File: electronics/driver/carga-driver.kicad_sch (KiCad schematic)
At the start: 74 parts, among them J1 USB2UART, J2 1.47 IPS LCD, J3 ConnBattery, J4 RTD_PT100, Q1 SS8050, Q2 SS8050, Q3 SS8050, SW1 RST, SW2 IN1, SW3 Boot, SW4 IN2, SW5 IN4, SW6 IN4, SW7 IN5, U1 CH340C, U2 ESP32-S3-WROOM-1, U3 TPS63001_SEPIC_3V3, U4 MAX31865xTP, U5 BQ24075RGT_DPPM, U6 HX711

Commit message: feat: create l298, mcp23017 driver module
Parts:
- removed C10: 22uF, Capacitor_SMD:C_0805_2012Metric_Pad1.18x1.45mm_HandSolder, symbol Device:C
- removed C11, C15: 1uF, Capacitor_SMD:C_0805_2012Metric_Pad1.18x1.45mm_HandSolder, symbol Device:C
- removed C12, C18, C19, C20, C3, C4, C5, C6, C7, C8, C9: 100nF, Capacitor_SMD:C_0805_2012Metric_Pad1.18x1.45mm_HandSolder, symbol Device:C
- removed C13, C16, C17: 10uF, Capacitor_SMD:C_0805_2012Metric_Pad1.18x1.45mm_HandSolder, symbol Device:C
- removed C14: 0.1uF, Capacitor_SMD:C_0805_2012Metric_Pad1.18x1.45mm_HandSolder, symbol Device:C
- removed C22, C23: 4.7uF, Capacitor_SMD:C_0805_2012Metric_Pad1.18x1.45mm_HandSolder, symbol Device:C
- removed D1: INDICATOR, LED_SMD:LED_1206_3216Metric_Pad1.42x1.75mm_HandSolder, symbol Device:LED
- removed D2: VDD, LED_SMD:LED_1206_3216Metric_Pad1.42x1.75mm_HandSolder, symbol Device:LED
- removed D3: green, LED_SMD:LED_0805_2012Metric_Pad1.15x1.40mm_HandSolder, symbol Device:LED
- removed D4: red, LED_SMD:LED_0805_2012Metric_Pad1.15x1.40mm_HandSolder, symbol Device:LED
- removed H1, H2, H3, H4: MountingHole, MountingHole:MountingHole_2mm, symbol Mechanical:MountingHole
- removed J1: USB2UART, Connector_USB:USB_C_Receptacle_GCT_USB4110, symbol Connector:USB_C_Receptacle_USB2.0_14P
- removed J2: 1.47 IPS LCD, Connector_PinHeader_2.54mm:PinHeader_1x08_P2.54mm_Vertical, symbol Connector_Generic:Conn_01x08
- removed J3: ConnBattery, Connector_PinHeader_2.54mm:PinHeader_1x03_P2.54mm_Vertical, symbol Connector_Generic:Conn_01x03
- removed J4: RTD_PT100, TerminalBlock_Phoenix:TerminalBlock_Phoenix_PT-1,5-3-5.0-H_1x03_P5.00mm_Horizontal, symbol Connector:Screw_Terminal_01x03
- removed JP1: 3_OR_2_Wire, Jumper:SolderJumper-3_P1.3mm_Open_RoundedPad1.0x1.5mm, symbol Jumper:SolderJumper_3_Open
- removed JP2: 2_Wire, Jumper:SolderJumper-2_P1.3mm_Open_TrianglePad1.0x1.5mm, symbol Jumper:SolderJumper_2_Open
- removed L1: 22uH 1A, Inductor_SMD:L_Bourns_SRP7028A_7.3x6.6mm, symbol Device:L
- removed Q1, Q2, Q3: SS8050, Package_TO_SOT_SMD:SOT-23_Handsoldering, symbol Transistor_BJT:BC817
- removed R1, R10, R13, R14, R2, R3, R4, R7, R8, R9: 1k, Resistor_SMD:R_0805_2012Metric_Pad1.20x1.40mm_HandSolder, symbol Device:R_US
- removed R11, R12: 10k, Resistor_SMD:R_0805_2012Metric_Pad1.20x1.40mm_HandSolder, symbol Device:R_US
- removed R15: 100, Resistor_SMD:R_0805_2012Metric_Pad1.20x1.40mm_HandSolder, symbol Device:R_US
- removed R16: 46.4K, Resistor_SMD:R_0805_2012Metric_Pad1.20x1.40mm_HandSolder, symbol Device:R_US
- removed R17: 2K2, Resistor_SMD:R_0805_2012Metric_Pad1.20x1.40mm_HandSolder, symbol Device:R_US
- removed R18: 1.13k, Resistor_SMD:R_0805_2012Metric_Pad1.20x1.40mm_HandSolder, symbol Device:R_US
- removed R19: 400 1%, Resistor_SMD:R_0805_2012Metric_Pad1.20x1.40mm_HandSolder, symbol Device:R_US
- removed R20, R21: 1K5, Resistor_SMD:R_0805_2012Metric_Pad1.20x1.40mm_HandSolder, symbol Device:R_US
- removed R5, R6: 5K1, Resistor_SMD:R_0805_2012Metric_Pad1.20x1.40mm_HandSolder, symbol Device:R_US
- removed SW1: RST, Button_Switch_SMD:SW_SPST_PTS810, symbol Switch:SW_Push
- removed SW2: IN1, Button_Switch_SMD:SW_SPST_Omron_B3FS-100xP, symbol Switch:SW_Push
- removed SW3: Boot, Button_Switch_SMD:SW_SPST_PTS810, symbol Switch:SW_Push
- removed SW4: IN2, Button_Switch_SMD:SW_SPST_Omron_B3FS-100xP, symbol Switch:SW_Push
- removed SW5, SW6: IN4, Button_Switch_SMD:SW_SPST_Omron_B3FS-100xP, symbol Switch:SW_Push
- removed SW7: IN5, Button_Switch_SMD:SW_SPST_Omron_B3FS-100xP, symbol Switch:SW_Push
- removed U1: CH340C, Package_SO:SOIC-16_3.9x9.9mm_P1.27mm, symbol Interface_USB:CH340C
- removed U2: ESP32-S3-WROOM-1, RF_Module:ESP32-S3-WROOM-1, symbol RF_Module:ESP32-S3-WROOM-1
- removed U3: TPS63001_SEPIC_3V3, Package_SON:Texas_DRC0010J_ThermalVias, symbol Regulator_Switching:TPS63001
- removed U4: MAX31865xTP, Package_DFN_QFN:TQFN-20-1EP_5x5mm_P0.65mm_EP3.25x3.25mm, symbol Sensor_Temperature:MAX31865xTP
- removed U5: BQ24075RGT_DPPM, Package_DFN_QFN:VQFN-16-1EP_3x3mm_P0.5mm_EP1.6x1.6mm, symbol Battery_Management:BQ24075RGT
- removed U6: HX711, Package_SO:SOIC-16_3.9x9.9mm_P1.27mm, symbol Analog_ADC:HX711
- added C21, C24, C25, C26: 100nF, Capacitor_SMD:C_0805_2012Metric_Pad1.18x1.45mm_HandSolder, symbol Device:C
- added D10, D11, D12, D13, D14, D15, D16, D17, D18, D19, D20, D5, D6, D7, D8, D9: 1N4007, Diode_THT:D_DO-41_SOD81_P10.16mm_Horizontal, symbol Diode:1N4007
- added J1: ServoConn, TerminalBlock_Phoenix:TerminalBlock_Phoenix_PT-1,5-3-5.0-H_1x03_P5.00mm_Horizontal, symbol Connector:Screw_Terminal_01x03
- added J10: LimitSw1, TerminalBlock_Phoenix:TerminalBlock_Phoenix_PT-1,5-4-5.0-H_1x04_P5.00mm_Horizontal, symbol Connector:Screw_Terminal_01x04
- added J11: LimitSw2, TerminalBlock_Phoenix:TerminalBlock_Phoenix_PT-1,5-4-5.0-H_1x04_P5.00mm_Horizontal, symbol Connector:Screw_Terminal_01x04
- added J12: LimitSwCommon, TerminalBlock_Phoenix:TerminalBlock_Phoenix_PT-1,5-2-5.0-H_1x02_P5.00mm_Horizontal, symbol Connector:Screw_Terminal_01x02
- added J2: DriverConn2, Connector_IDC:IDC-Header_2x05_P2.54mm_Vertical, symbol Connector_Generic:Conn_02x05_Odd_Even
- added J5: DriverConn, Connector_IDC:IDC-Header_2x05_P2.54mm_Vertical, symbol Connector_Generic:Conn_02x05_Odd_Even
- added J7: MotorConn2_3, TerminalBlock_Phoenix:TerminalBlock_Phoenix_PT-1,5-4-5.0-H_1x04_P5.00mm_Horizontal, symbol Connector:Screw_Terminal_01x04
- added J8: SolenoidConn, TerminalBlock_Phoenix:TerminalBlock_Phoenix_PT-1,5-2-5.0-H_1x02_P5.00mm_Horizontal, symbol Connector:Screw_Terminal_01x02
- added J9: MotorConn1, TerminalBlock_Phoenix:TerminalBlock_Phoenix_PT-1,5-2-5.0-H_1x02_P5.00mm_Horizontal, symbol Connector:Screw_Terminal_01x02
- added R22, R23, R24: 4K7, Resistor_SMD:R_0805_2012Metric_Pad1.20x1.40mm_HandSolder, symbol Device:R_US
- added R25, R26, R27, R28: 1, Resistor_SMD:R_0805_2012Metric_Pad1.20x1.40mm_HandSolder, symbol Device:R_US
- added U10, U7: L298HN, Package_TO_SOT_THT:TO-220-15_P2.54x2.54mm_StaggerOdd_Lead5.84mm_TabDown, symbol Driver_Motor:L298HN
- added U8: MCP23017_SS, Package_SO:SSOP-28_5.3x10.2mm_P0.65mm, symbol Interface_Expansion:MCP23017_SS
- added U9: TXS0108EPW, Package_SO:TSSOP-20_4.4x6.5mm_P0.65mm, symbol Logic_LevelTranslator:TXS0108EPW
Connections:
- net EN is gone; now on net +3.3V: C2.1
- net +3.3V: now also J5.1 (Pin_1), R22.1, R23.1, U8.16 (A1), U8.17 (A2), U8.18 (~{RESET}), U9.2 (VCCA)
- net GND: now also C21.2, C24.2, C25.2, C26.2, D10.2 (A), D11.2 (A), D12.2 (A), D14.2 (A), D16.2 (A), D18.2 (A), D20.2 (A), D7.2 (A), J1.3 (Pin_3), J12.2 (Pin_2), J5.10 (Pin_10), R24.2, R25.2, R26.2, R27.2, R28.2, U10.8 (GND), U7.8 (GND), U8.10 (VSS), U8.15 (A0), U9.11 (GND)
- net IN1 renamed +5V
- net +5V: now also C24.1, C26.1, J12.1 (Pin_1), J5.2 (Pin_2), U10.9 (Vss), U7.9 (Vss), U8.9 (VDD), U9.19 (VCCB)
- new net: R28.1, U10.15 (SENSE_B)
- new net: D5.2 (A), D7.1 (K), J8.1 (Pin_1), U7.2 (OUT1)
- new net: D10.1 (K), D6.2 (A), J8.2 (Pin_2), U7.3 (OUT2)
- new net: R24.1, U9.10 (OE)
- new net: D15.2 (A), D16.1 (K), J7.2 (Pin_2), U10.3 (OUT2)
- new net: D13.2 (A), D14.1 (K), J7.1 (Pin_1), U10.2 (OUT1)
- new net: D17.2 (A), D18.1 (K), J7.3 (Pin_3), U10.13 (OUT3)
- new net: D19.2 (A), D20.1 (K), J7.4 (Pin_4), U10.14 (OUT4)
- new net: U7.5 (IN1), U8.1 (GPB0)
- new net: U7.7 (IN2), U8.2 (GPB1)
- new net: U7.10 (IN3), U8.3 (GPB2)
- new net: U7.12 (IN4), U8.4 (GPB3)
- new net: U10.5 (IN1), U8.5 (GPB4)
- new net: U10.7 (IN2), U8.6 (GPB5)
- new net: U10.10 (IN3), U8.7 (GPB6)
- new net: U10.12 (IN4), U8.8 (GPB7)
- new net: R25.1, U7.1 (SENSE_A)
- new net: D11.1 (K), D8.2 (A), J9.1 (Pin_1), U7.13 (OUT3)
- new net: D12.1 (K), D9.2 (A), J9.2 (Pin_2), U7.14 (OUT4)
- new net: R26.1, U7.15 (SENSE_B)
- new net: R27.1, U10.1 (SENSE_A)
- new net ENA1: U7.6 (EnA), U9.20 (B1)
- new net ENA2: U10.6 (EnA), U9.17 (B3)
- new net ENB1: U7.11 (EnB), U9.18 (B2)
- new net ENB2: U10.11 (EnB), U9.16 (B4)
- new net I2C_SCK: J5.8 (Pin_8), R23.2, U8.12 (SCK)
- new net I2C_SDA: J5.6 (Pin_6), R22.2, U8.13 (SDA)
- new net IN_ENA1: J5.3 (Pin_3), U9.1 (A1)
- new net IN_ENA2: J5.7 (Pin_7), U9.4 (A3)
- new net IN_ENB1: J5.5 (Pin_5), U9.3 (A2)
- new net IN_ENB2: J5.9 (Pin_9), U9.5 (A4)
- new net IN_SERVO: J2.3 (Pin_3), U9.6 (A5)
- new net LIMIT_SW1: J10.1 (Pin_1), U8.21 (GPA0)
- new net LIMIT_SW2: J10.2 (Pin_2), U8.22 (GPA1)
- new net LIMIT_SW3: J10.3 (Pin_3), U8.23 (GPA2)
- new net LIMIT_SW4: J10.4 (Pin_4), U8.24 (GPA3)
- new net LIMIT_SW5: J11.1 (Pin_1), U8.25 (GPA4)
- new net LIMIT_SW6: J11.2 (Pin_2), U8.26 (GPA5)
- new net LIMIT_SW7: J11.3 (Pin_3), U8.27 (GPA6)
- new net LIMIT_SW8: J11.4 (Pin_4), U8.28 (GPA7)
- new net SERVO: J1.2 (Pin_2), U9.15 (B5)
- new net VM: C21.1, C25.1, D13.1 (K), D15.1 (K), D17.1 (K), D19.1 (K), D5.1 (K), D6.1 (K), D8.1 (K), D9.1 (K), J5.4 (Pin_4), U10.4 (Vs), U7.4 (Vs)
- new net VSER: J1.1 (Pin_1), J2.1 (Pin_1)
- no-connect marks 24 -> 8
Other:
- note added: "Hardware Address Decoder 110 -> 0x06"
- note added: "MCP23017"
- note added: "TODO think about rsense power"
- note removed: "3 Wire to Force+ 2/4 Wire to GND Connect 2_Wire if use 2/4 Wire"
- note removed: "DPPM"
- note removed: "ESP32-S3-WROOM-1"
- note removed: "GND VCC SCL SDA RES DC CS BLK"
- note removed: "Program Fast-Charge Safety Timer (TMR): RTMR = tMAXCHG / (10 × KTMR ) KTMR = 48 s/kΩ from the electrical characteristics table. RTMR = (6.25 hr × 3600 s/hr) / (10 × 48 s/kΩ) = 46.8 kΩ -> 46.4 kΩ"
- note removed: "Program the Fast Charge Current (ISET): RISET = KISET / ICHG KISET = 890 AΩ from the electrical characteristics table. RISET = 890 AΩ / 0.8 A = 1.1125 kΩ -> 1.13 kΩ"
- note removed: "SEPIC 3.3V"
- note removed: "dynamic power path management"
- note removed: "miso - Also known as q, this is the input of the serial stream into the ESP32 mosi - Also known as d, this is the output of the serial stream from the ESP32 sclk - Clock signal. Each data bit is clocked out or in on the positive or negative edge of this signal quadwp - Write Protect signal. Only used for 4-bit (qio/qout) transactions. quadhd - Hold signal. Only used for 4-bit (qio/qout) transacti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"
- title: (none) -> Carga Driver Module

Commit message: feat: add ADuM1234 and IRLZ44N for driving Solenoid
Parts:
- removed J8: SolenoidConn, TerminalBlock_Phoenix:TerminalBlock_Phoenix_PT-1,5-2-5.0-H_1x02_P5.00mm_Horizontal, symbol Connector:Screw_Terminal_01x02
- removed J9: MotorConn1, TerminalBlock_Phoenix:TerminalBlock_Phoenix_PT-1,5-2-5.0-H_1x02_P5.00mm_Horizontal, symbol Connector:Screw_Terminal_01x02
- removed R25, R26, R27, R28: 1, Resistor_SMD:R_0805_2012Metric_Pad1.20x1.40mm_HandSolder, symbol Device:R_US
- added D1, D2: 1N4007, Diode_THT:D_DO-41_SOD81_P10.16mm_Horizontal, symbol Diode:1N4007
- added J13, J3: SolenoidConn, TerminalBlock_Phoenix:TerminalBlock_Phoenix_PT-1,5-2-5.0-H_1x02_P5.00mm_Horizontal, symbol Connector:Screw_Terminal_01x02
- added J14: MotorConn1_2, TerminalBlock_Phoenix:TerminalBlock_Phoenix_PT-1,5-4-5.0-H_1x04_P5.00mm_Horizontal, symbol Connector:Screw_Terminal_01x04
- added J4: VDDBConn, TerminalBlock_Phoenix:TerminalBlock_Phoenix_PT-1,5-2-5.0-H_1x02_P5.00mm_Horizontal, symbol Connector:Screw_Terminal_01x02
- added J6: VDDAConn, TerminalBlock_Phoenix:TerminalBlock_Phoenix_PT-1,5-2-5.0-H_1x02_P5.00mm_Horizontal, symbol Connector:Screw_Terminal_01x02
- added Q1, Q2: IRLZ44N, Package_TO_SOT_THT:TO-220-3_Horizontal_TabDown, symbol Transistor_FET:IRLZ44N
- added U1: ADUM1234BRWZ, Package_SO:SOIC-16W_7.5x10.3mm_P1.27mm, symbol ADUM1234BRWZ:ADUM1234BRWZ
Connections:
- net +5V: now also U1.3 (VDD1_2), U1.8 (VDD1)
- net GND: now also U10.1 (SENSE_A), U10.15 (SENSE_B), U7.1 (SENSE_A), U7.15 (SENSE_B), U1.4 (GND1), U1.5 (DISABLE)
- net at D5.2 (A), D7.1 (K), U7.2 (OUT1): now also J14.1 (Pin_1)
- net at D10.1 (K), D6.2 (A), U7.3 (OUT2): now also J14.2 (Pin_2)
- net SOL_VIB: now reaches U9.13 (B7)
- net SOL_VIB: now also U1.2 (VIB)
- net SOL_VIA: now reaches U9.14 (B6)
- net SOL_VIA: now also U1.1 (VIA)
- net IN_SOL_VIA: now reaches U9.7 (A6)
- net IN_SOL_VIA: now also J2.5 (Pin_5)
- net IN_SOL_VIB: now reaches U9.8 (A7)
- net IN_SOL_VIB: now also J2.7 (Pin_7)
- net at D11.1 (K), D8.2 (A), U7.13 (OUT3): now also J14.3 (Pin_3)
- net at D12.1 (K), D9.2 (A), U7.14 (OUT4): now also J14.4 (Pin_4)
- net GNDA: now reaches J2.10 (Pin_10)
- net GNDA: now also J6.2 (Pin_2), Q2.3 (S), U1.14 (GNDA)
- net VDDA: now reaches J2.2 (Pin_2)
- net VDDA: now also D2.1 (K), J13.1 (Pin_1), J6.1 (Pin_1), U1.16 (VDDA)
- net VDDB: now reaches J2.4 (Pin_4)
- net VDDB: now also D1.1 (K), J3.1 (Pin_1), J4.1 (Pin_1), U1.11 (VDDB)
- net GNDB: now reaches J2.8 (Pin_8)
- net GNDB: now also J4.2 (Pin_2), Q1.3 (S), U1.9 (GNDB)
- new net: D1.2 (A), J3.2 (Pin_2), Q1.2 (D)
- new net: Q1.1 (G), U1.10 (VOB)
- new net: D2.2 (A), J13.2 (Pin_2), Q2.2 (D)
- new net: Q2.1 (G), U1.15 (VOA)
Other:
- note removed: "TODO think about rsense power"
- moved on the sheet: C1, C2, C21, C24, C25, C26, D10, D11, D12, D13, D14, D15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

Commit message: feat: add voltage regulator to carga main
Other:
- moved on the sheet: C1, C2, C21, C24, C25, C26, D1, D10, D11, D12, D13, D14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

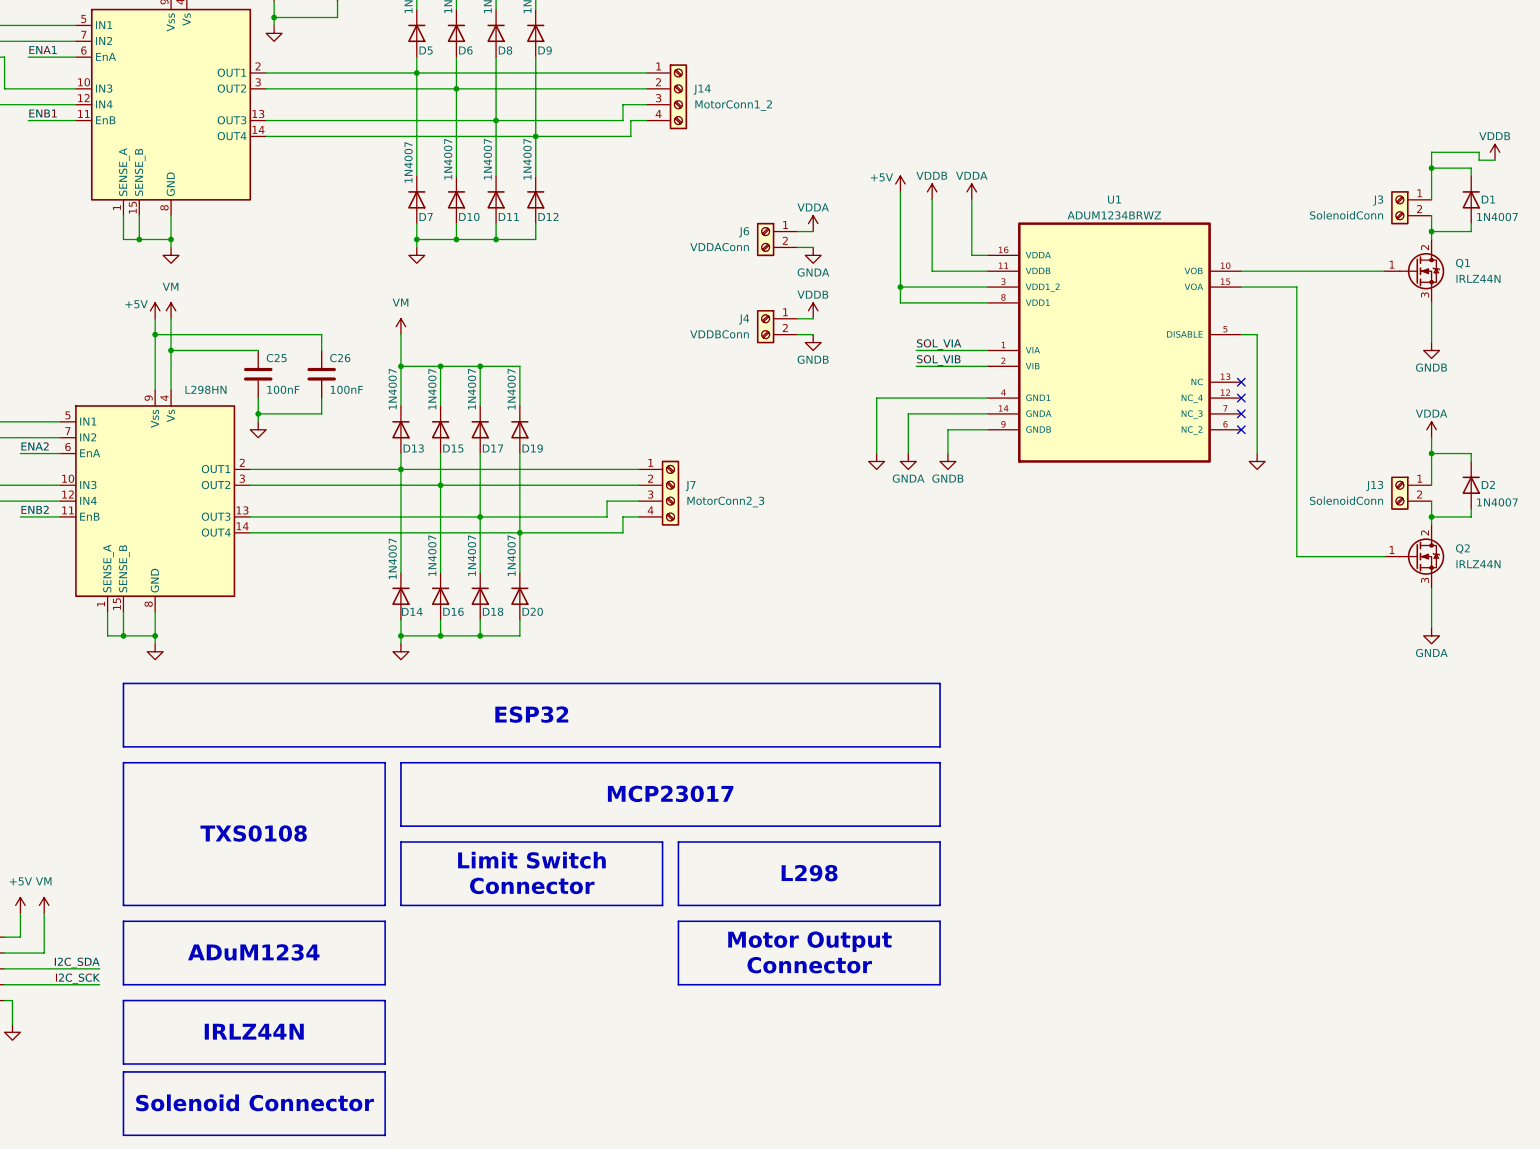
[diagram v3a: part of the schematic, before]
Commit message: chore: flip mosi miso pin
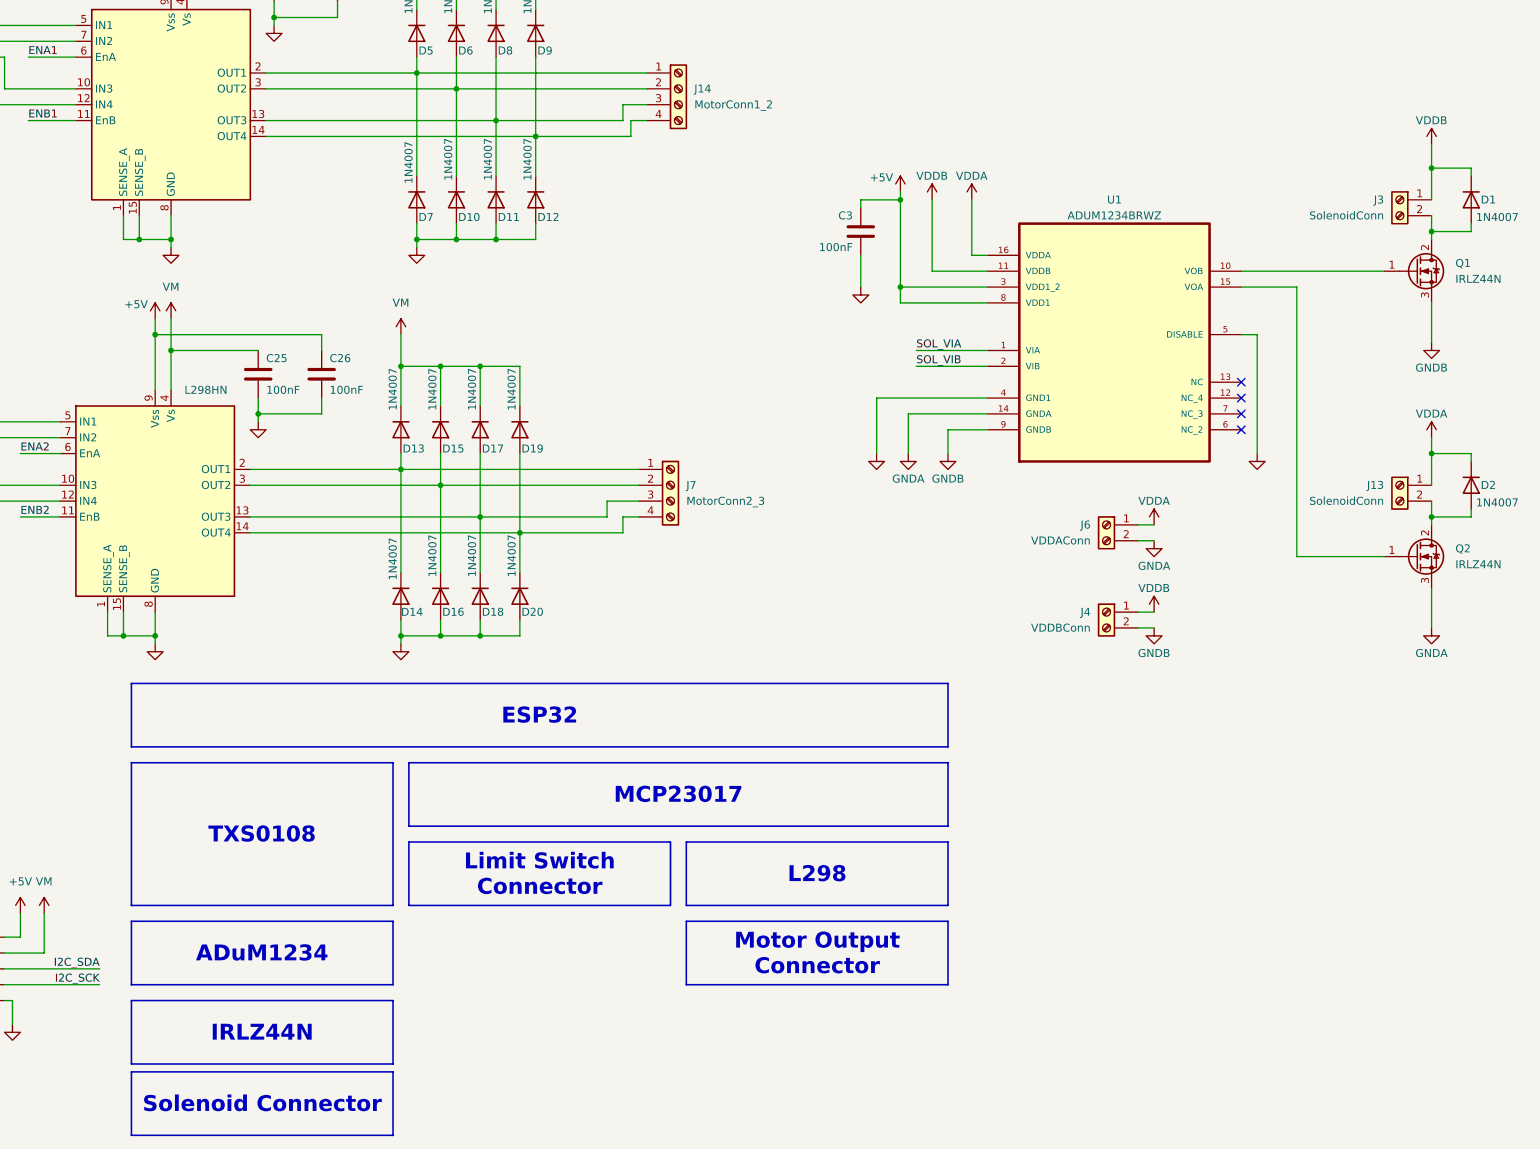
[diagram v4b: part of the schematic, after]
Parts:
- added C3: 100nF, Capacitor_SMD:C_0805_2012Metric_Pad1.18x1.45mm_HandSolder, symbol Device:C
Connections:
- net +5V: now also C3.1
- net GND: now also C3.2
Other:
- moved on the sheet: J4, J6
